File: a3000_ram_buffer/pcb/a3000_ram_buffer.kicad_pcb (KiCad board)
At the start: 2 copper layers, 167.6 x 43.2 mm, 29 parts

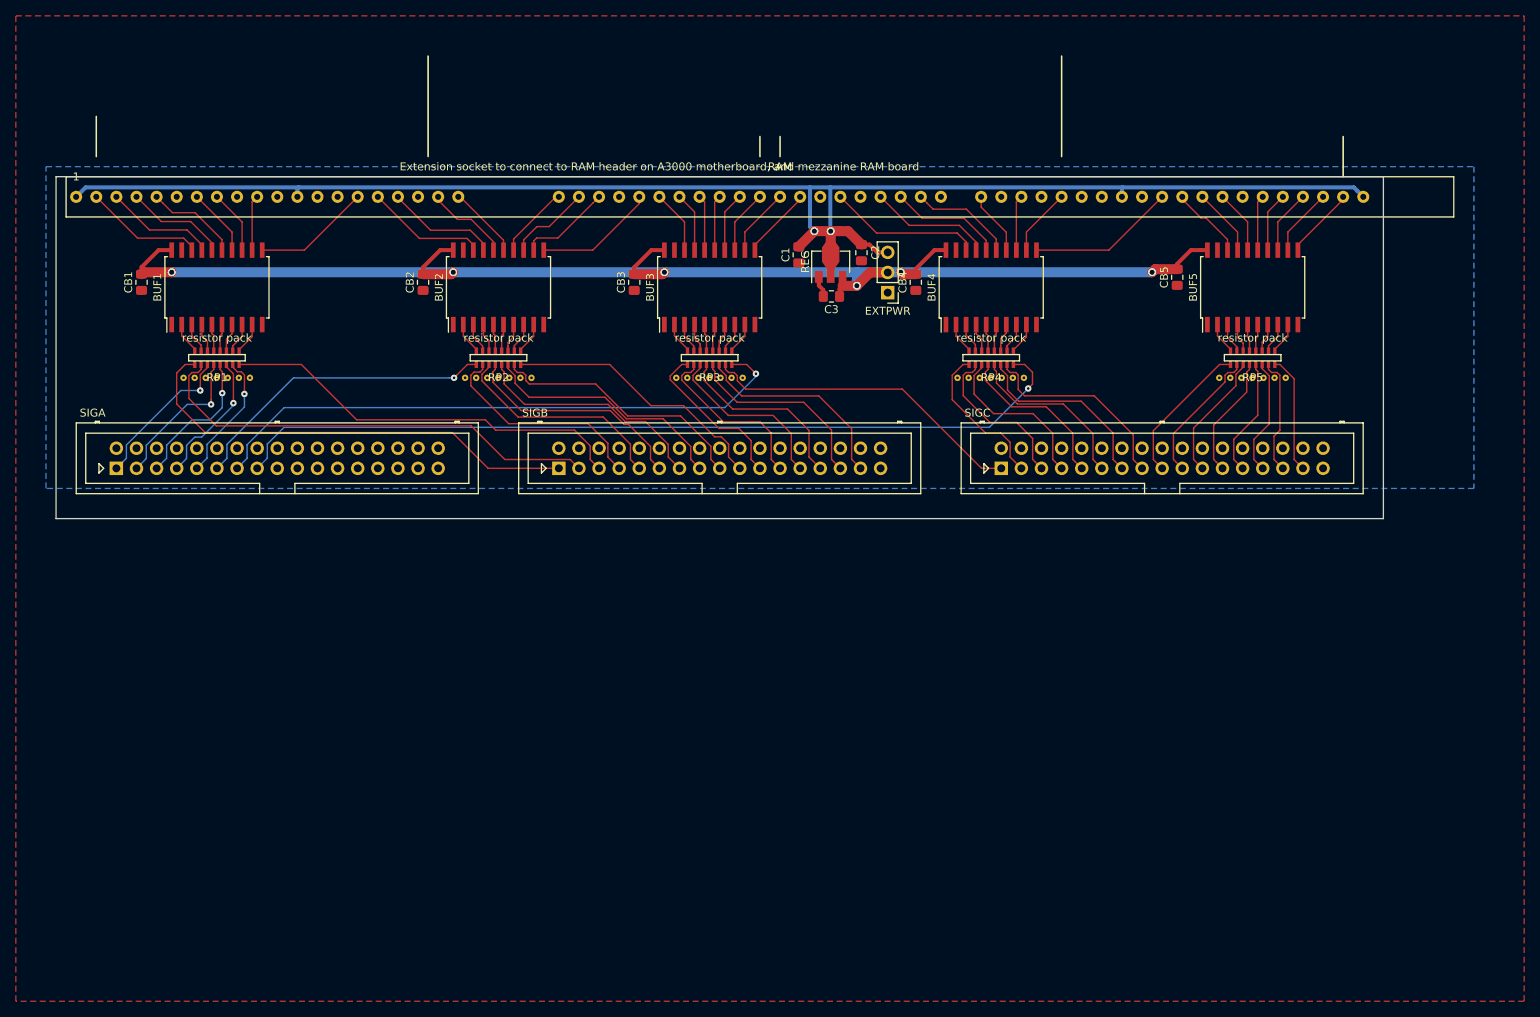
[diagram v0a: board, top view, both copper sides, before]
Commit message: Mainly silkscreen work, some tracking
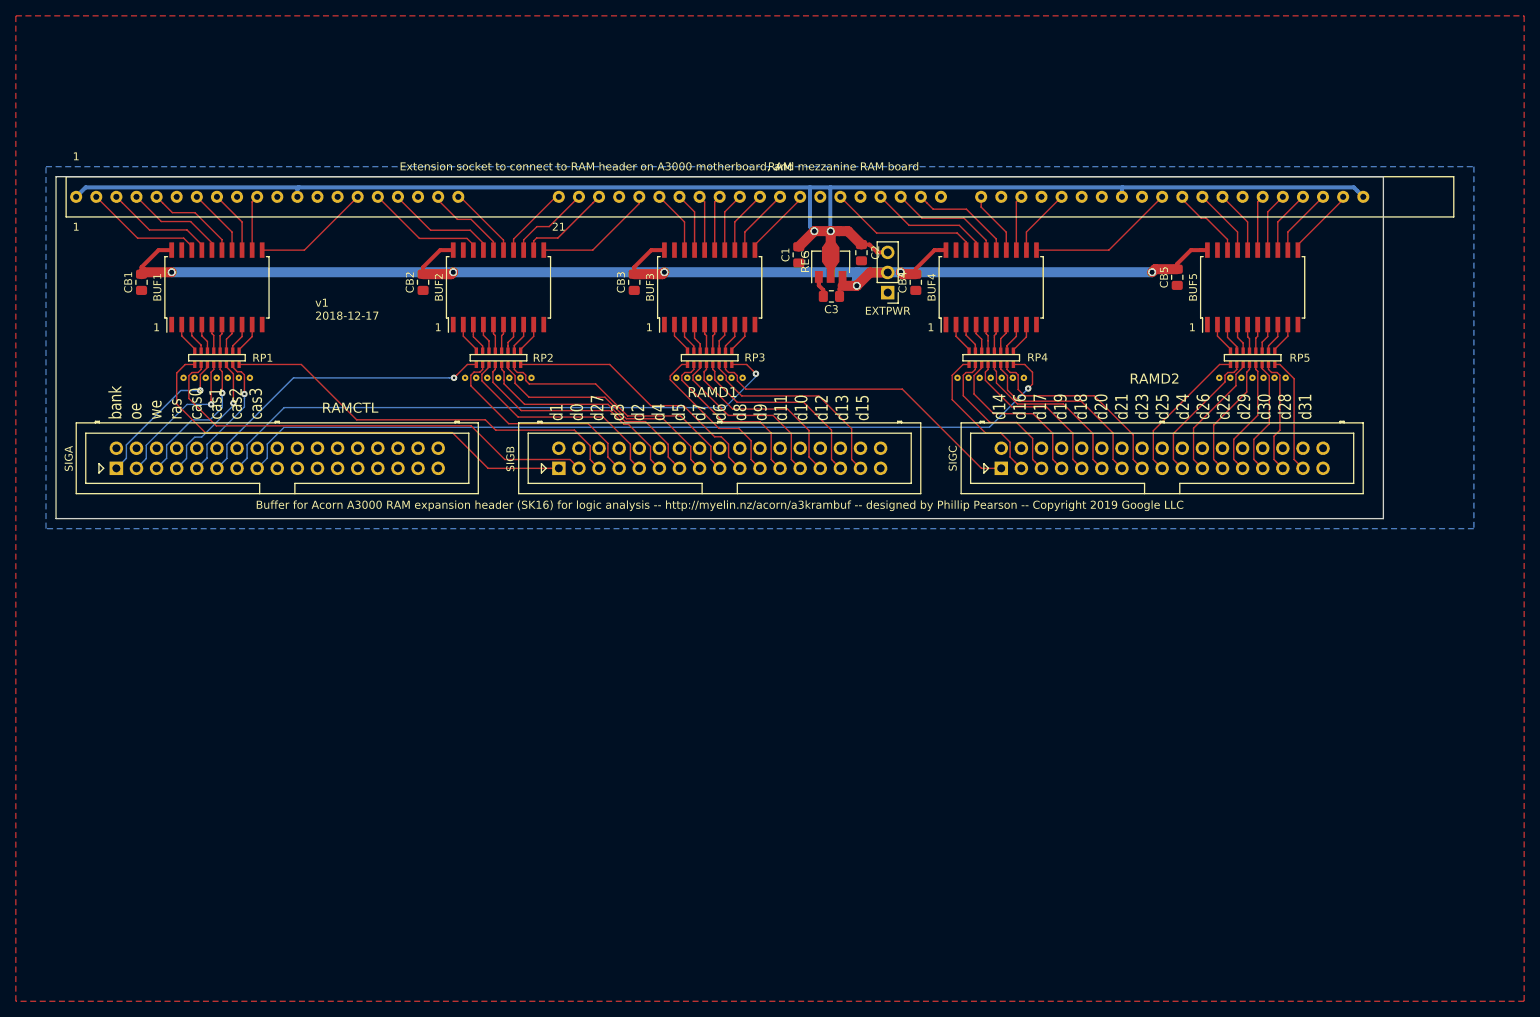
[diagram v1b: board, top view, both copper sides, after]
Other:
- board text added: "1"
- board text added: "21"
- board text added: "Buffer for Acorn A3000 RAM expansion header (SK16) for logic analysis -- http://myelin.nz/acorn/a3krambuf -- designed by Phillip Pearson -- Copyright 2019 Google LLC"
- board text added: "RAMCTL"
- board text added: "RAMD1"
- board text added: "RAMD2"
- board text added: "bank oe we ras cas0 cas1 cas2 cas3"
- board text added: "d1 d0 d27 d3 d2 d4 d5 d7 d6 d8 d9 d11 d10 d12 d13 d15"
- board text added: "d14 d16 d17 d19 d18 d20 d21 d23 d25 d24 d26 d22 d29 d30 d28 d31"
- board text added: "myelin.nz"
- board text added: "v1 2018-12-17"
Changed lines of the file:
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@@
   (general
     (thickness 1.6)
-    (drawings 10)
+    (drawings 20)
     (tracks 719)
     (zones 0)
@@
   )
   (setup
-    (last_trace_width 0.508)
+    (last_trace_width 0.1778)
     (user_trace_width 0.254)
     (user_trace_width 0.508)
@@
     (at 55.88 73.66 90)
     (descr "Bourns CAT16-J8 resistor array (8 isolated resistors, 0.8mm pitch, concave)")
-    (fp_text reference RP1 (at -2.5 0 -180) (layer F.SilkS)
-      (effects (font (size 1 1) (thickness 0.15)))
-    )
-    (fp_text value "resistor pack" (at 2.5 0 -180) (layer F.SilkS)
+    (fp_text reference RP1 (at -0.04064 5.78866 -180) (layer F.SilkS)
+      (effects (font (size 1 1) (thickness 0.15)))
+    )
+    (fp_text value "resistor pack" (at 2.5 0 180) (layer F.SilkS) hide
       (effects (font (size 1 1) (thickness 0.15)))
     )
@@
     (at 91.44 73.66 90)
     (descr "Bourns CAT16-J8 resistor array (8 isolated resistors, 0.8mm pitch, concave)")
-    (fp_text reference RP2 (at -2.5 0 -180) (layer F.SilkS)
-      (effects (font (size 1 1) (thickness 0.15)))
-    )
-    (fp_text value "resistor pack" (at 2.5 0 -180) (layer F.SilkS)
+    (fp_text reference RP2 (at -0.04318 5.6515 -180) (layer F.SilkS)
+      (effects (font (size 1 1) (thickness 0.15)))
+    )
+    (fp_text value "resistor pack" (at 2.5 0 180) (layer F.SilkS) hide
       (effects (font (size 1 1) (thickness 0.15)))
     )
@@
     (at 118.11 73.66 90)
     (descr "Bourns CAT16-J8 resistor array (8 isolated resistors, 0.8mm pitch, concave)")
-    (fp_text reference RP3 (at -2.5 0 -180) (layer F.SilkS)
-      (effects (font (size 1 1) (thickness 0.15)))
-    )
-    (fp_text value "resistor pack" (at 2.5 0 -180) (layer F.SilkS)
+    (fp_text reference RP3 (at 0 5.71246 -180) (layer F.SilkS)
+      (effects (font (size 1 1) (thickness 0.15)))
+    )
+    (fp_text value "resistor pack" (at 2.5 0 180) (layer F.SilkS) hide
       (effects (font (size 1 1) (thickness 0.15)))
     )
@@
     (at 153.67 73.66 90)
     (descr "Bourns CAT16-J8 resistor array (8 isolated resistors, 0.8mm pitch, concave)")
-    (fp_text reference RP4 (at -2.5 0 -180) (layer F.SilkS)
-      (effects (font (size 1 1) (thickness 0.15)))
-    )
-    (fp_text value "resistor pack" (at 2.5 0 -180) (layer F.SilkS)
+    (fp_text reference RP4 (at 0.0127 5.85724 -180) (layer F.SilkS)
+      (effects (font (size 1 1) (thickness 0.15)))
+    )
+    (fp_text value "resistor pack" (at 2.5 0 180) (layer F.SilkS) hide
       (effects (font (size 1 1) (thickness 0.15)))
     )
@@
       (effects (font (size 1 1) (thickness 0.15)))
     )
-    (fp_text user 1 (at -81.28 -2.54) (layer F.SilkS)
+    (fp_text user 1 (at -81.28 -5.08) (layer F.SilkS)
       (effects (font (size 1 1) (thickness 0.15)))
     )
@@
     (at 186.69 73.66 90)
     (descr "Bourns CAT16-J8 resistor array (8 isolated resistors, 0.8mm pitch, concave)")
-    (fp_text reference RP5 (at -2.5 0 180) (layer F.SilkS)
-      (effects (font (size 1 1) (thickness 0.15)))
-    )
-    (fp_text value "resistor pack" (at 2.5 0 180) (layer F.SilkS)
+    (fp_text reference RP5 (at -0.03556 5.97154 180) (layer F.SilkS)
+      (effects (font (size 1 1) (thickness 0.15)))
+    )
+    (fp_text value "resistor pack" (at 2.5 0 180) (layer F.SilkS) hide
       (effects (font (size 1 1) (thickness 0.15)))
     )
@@
     (descr http://www.farnell.com/datasheets/1520732.pdf)
     (tags "connector multicomp MC9A MC9A12")
-    (fp_text reference SIGA (at -3 -7) (layer F.SilkS)
+    (fp_text reference SIGA (at -5.98678 -1.21158 90) (layer F.SilkS)
       (effects (font (size 1 1) (thickness 0.15)))
     )
@@
     (descr http://www.farnell.com/datasheets/1520732.pdf)
     (tags "connector multicomp MC9A MC9A12")
-    (fp_text reference SIGB (at -3 -7) (layer F.SilkS)
+    (fp_text reference SIGB (at -6.08838 -1.18618 90) (layer F.SilkS)
       (effects (font (size 1 1) (thickness 0.15)))
     )
@@
     (descr http://www.farnell.com/datasheets/1520732.pdf)
     (tags "connector multicomp MC9A MC9A12")
-    (fp_text reference SIGC (at -3 -7) (layer F.SilkS)
+    (fp_text reference SIGC (at -6.096 -1.26238 90) (layer F.SilkS)
       (effects (font (size 1 1) (thickness 0.15)))
     )
@@
     )
   )
+  (gr_text 1 (at 48.26 69.85) (layer F.SilkS)
+    (effects (font (size 1 1) (thickness 0.2)))
+  )
+  (gr_text 1 (at 83.82 69.85) (layer F.SilkS)
+    (effects (font (size 1 1) (thickness 0.2)))
+  )
+  (gr_text 1 (at 110.49 69.85) (layer F.SilkS)
+    (effects (font (size 1 1) (thickness 0.2)))
+  )
+  (gr_text 21 (at 99.06 57.15) (layer F.SilkS)
+    (effects (font (size 1 1) (thickness 0.2)))
+  )
+  (gr_text 1 (at 38.1 57.15) (layer F.SilkS)
+    (effects (font (size 1 1) (thickness 0.2)))
+  )
+  (gr_text 1 (at 146.05 69.85) (layer F.SilkS)
+    (effects (font (size 1 1) (thickness 0.2)))
+  )
+  (gr_text 1 (at 179.07 69.85) (layer F.SilkS)
+    (effects (font (size 1 1) (thickness 0.2)))
+  )
+  (gr_text "v1\n2018-12-17" (at 68.2879 67.56654) (layer F.SilkS)
+    (effects (font (size 1.016 1.016) (thickness 0.1778)) (justify left))
+  )
+  (gr_text "Buffer for Acorn A3000 RAM expansion header (SK16) for logic analysis -- http://myelin.nz/acorn/a3krambuf -- designed by Phillip Pearson -- Copyright 2019 Google LLC" (at 119.3927 92.27058) (layer F.SilkS)
+    (effects (font (size 1.016 1.016) (thickness 0.1778)))
+  )
+  (gr_text RAMD2 (at 174.3075 76.34224) (layer F.SilkS)
+    (effects (font (size 1.27 1.27) (thickness 0.1524)))
+  )
+  (gr_text RAMD1 (at 118.47576 78.04912) (layer F.SilkS)
+    (effects (font (size 1.27 1.27) (thickness 0.1524)))
+  )
+  (gr_text RAMCTL (at 72.69226 80.02016) (layer F.SilkS)
+    (effects (font (size 1.27 1.27) (thickness 0.1524)))
+  )
+  (gr_text "d14\nd16\nd17\nd19\nd18\nd20\nd21\nd23\nd25\nd24\nd26\nd22\nd29\nd30\nd28\nd31" (at 174.03572 81.50606 90) (layer F.SilkS)
+    (effects (font (size 1.6002 1.27) (thickness 0.1524)) (justify left))
+  )
+  (gr_text "d1\nd0\nd27\nd3\nd2\nd4\nd5\nd7\nd6\nd8\nd9\nd11\nd10\nd12\nd13\nd15\n" (at 118.11508 81.65084 90) (layer F.SilkS)
+    (effects (font (size 1.6002 1.27) (thickness 0.1524)) (justify left))
+  )
+  (gr_text "bank\noe\nwe\nras\ncas0\ncas1\ncas2\ncas3" (at 51.95062 81.48066 90) (layer F.SilkS)
+    (effects (font (size 1.5748 1.27) (thickness 0.1524)) (justify left))
+  )
+  (gr_text myelin.nz (at 119.4308 71.48068) (layer B.SilkS)
+    (effects (font (size 5.08 5.08) (thickness 1.27) italic) (justify mirror))
+  )
   (gr_line (start 35.56 93.98) (end 35.56 50.8) (layer Edge.Cuts) (width 0.1))
   (gr_line (start 203.2 93.98) (end 35.56 93.98) (layer Edge.Cuts) (width 0.1))
   (gr_line (start 203.2 50.8) (end 203.2 93.98) (layer Edge.Cuts) (width 0.1))
   (gr_line (start 35.56 50.8) (end 203.2 50.8) (layer Edge.Cuts) (width 0.1))
-  (gr_line (start 162.56 48.26) (end 162.56 35.56) (layer F.SilkS) (width 0.2))
-  (gr_line (start 82.55 48.26) (end 82.55 35.56) (layer F.SilkS) (width 0.2))
-  (gr_line (start 40.64 48.26) (end 40.64 43.18) (layer F.SilkS) (width 0.2))
-  (gr_line (start 124.46 48.26) (end 124.46 45.72) (layer F.SilkS) (width 0.2))
-  (gr_line (start 127 48.26) (end 127 45.72) (layer F.SilkS) (width 0.2))
-  (gr_line (start 198.12 50.8) (end 198.12 45.72) (layer F.SilkS) (width 0.2))
   (segment (start 132.4647 65.11554) (end 131.89572 64.54656) (width 0.508) (layer F.Cu) (net 1))
   (segment (start 131.89572 64.54656) (end 131.89572 64.25438) (width 0.508) (layer F.Cu) (net 1))
@@
     (polygon
       (pts
-        (xy 34.29 49.53) (xy 214.63 49.53) (xy 214.63 90.17) (xy 34.29 90.17)
+        (xy 34.29 49.53) (xy 214.63 49.53) (xy 214.63 95.25) (xy 34.29 95.25)
       )
     )

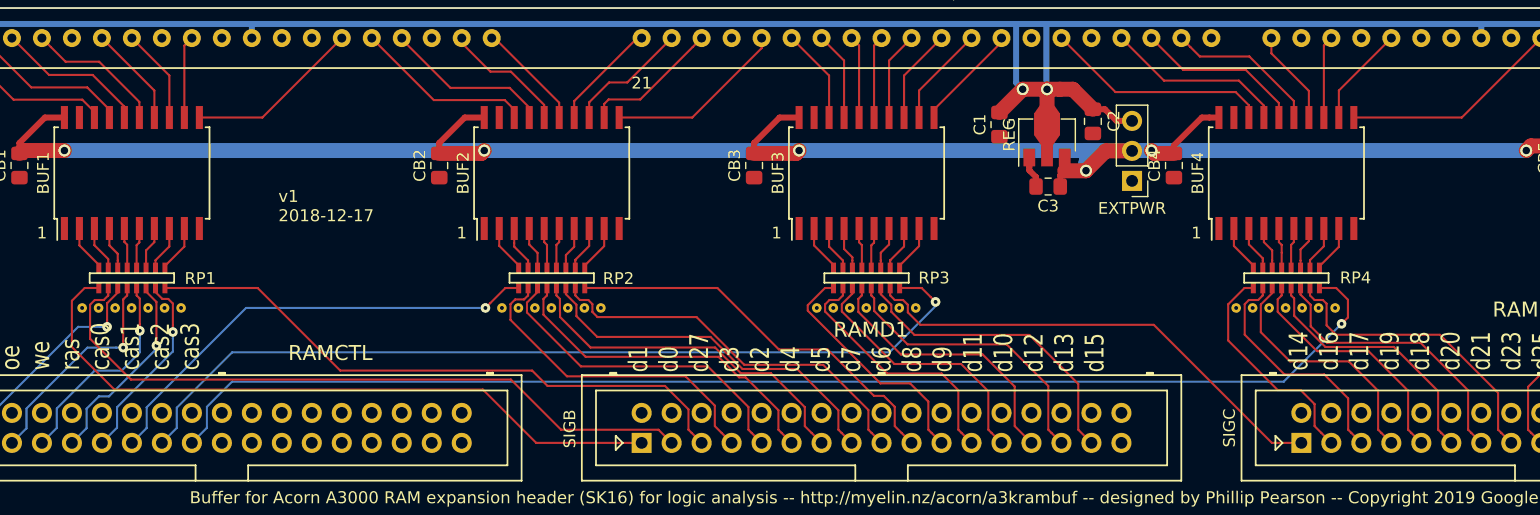
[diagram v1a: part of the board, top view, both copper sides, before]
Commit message: Tidied tracks and silkscreen
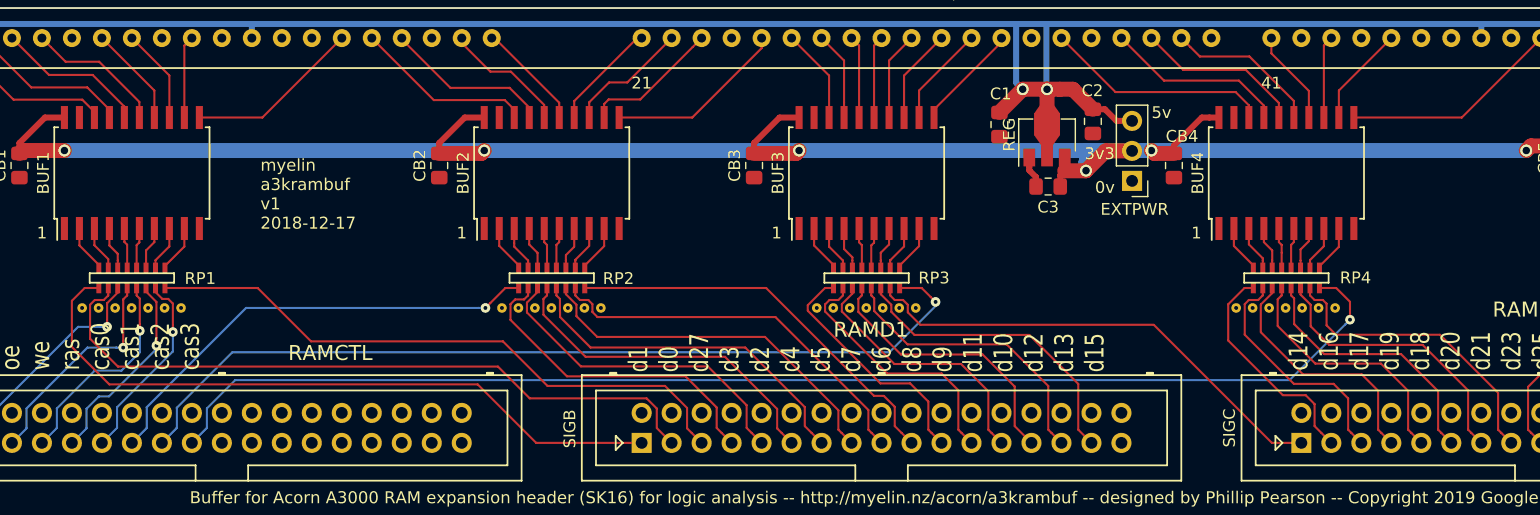
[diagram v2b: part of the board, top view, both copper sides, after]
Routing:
- net ram_D0_term: track 58.3 -> 59.3 mm
- net ram_D18_term: track 20.9 -> 21.6 mm
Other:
- board text added: "0v"
- board text added: "3v3"
- board text added: "41"
- board text added: "5v"
- board text added: "myelin a3krambuf v1 2018-12-17"
- board text removed: "v1 2018-12-17"

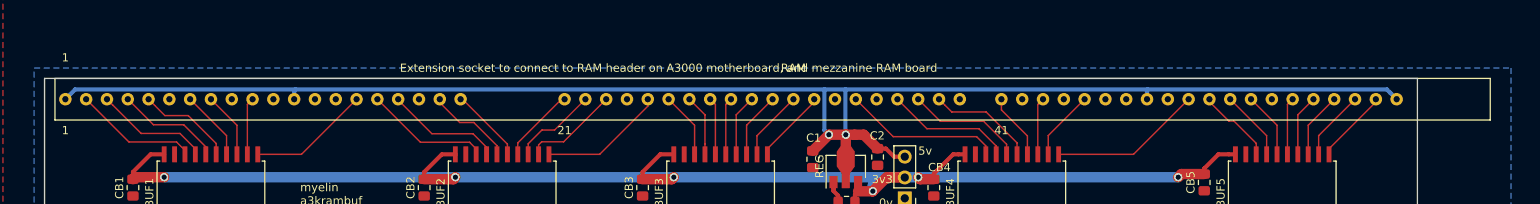
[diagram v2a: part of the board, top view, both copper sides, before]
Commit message: Updated RAM connector per cmorley's advice on Stardot: moved the left block of 20 pins 25 mils right
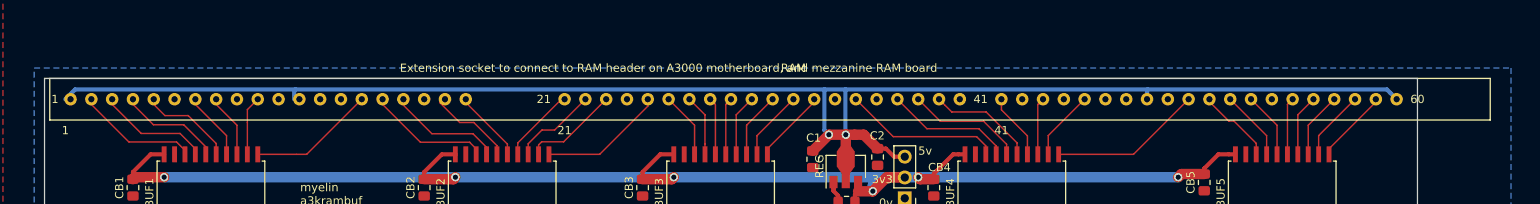
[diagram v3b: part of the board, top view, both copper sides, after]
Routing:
- net ram_D27: track 14.9 -> 15.5 mm
